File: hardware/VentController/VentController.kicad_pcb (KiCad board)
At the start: 2 copper layers, 18 parts, among them J1 AM2301B, J2 Conn_01x02, Q1 Q_NPN_EBC, U1 ATtiny85-20P

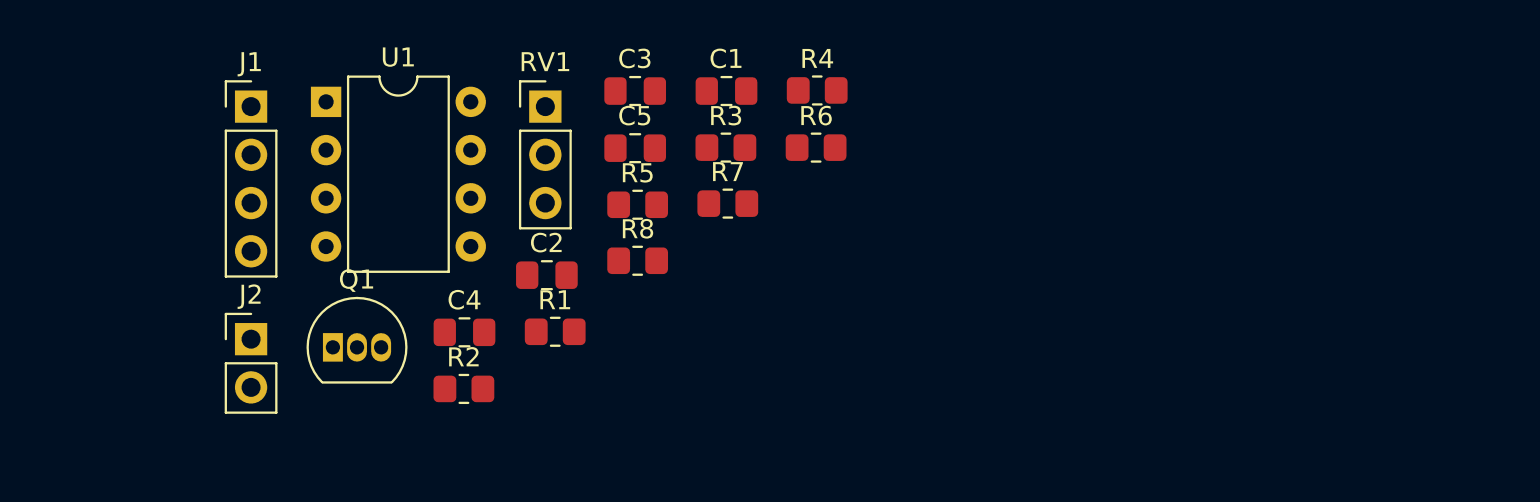
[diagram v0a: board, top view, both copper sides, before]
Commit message: Set pcb board edges
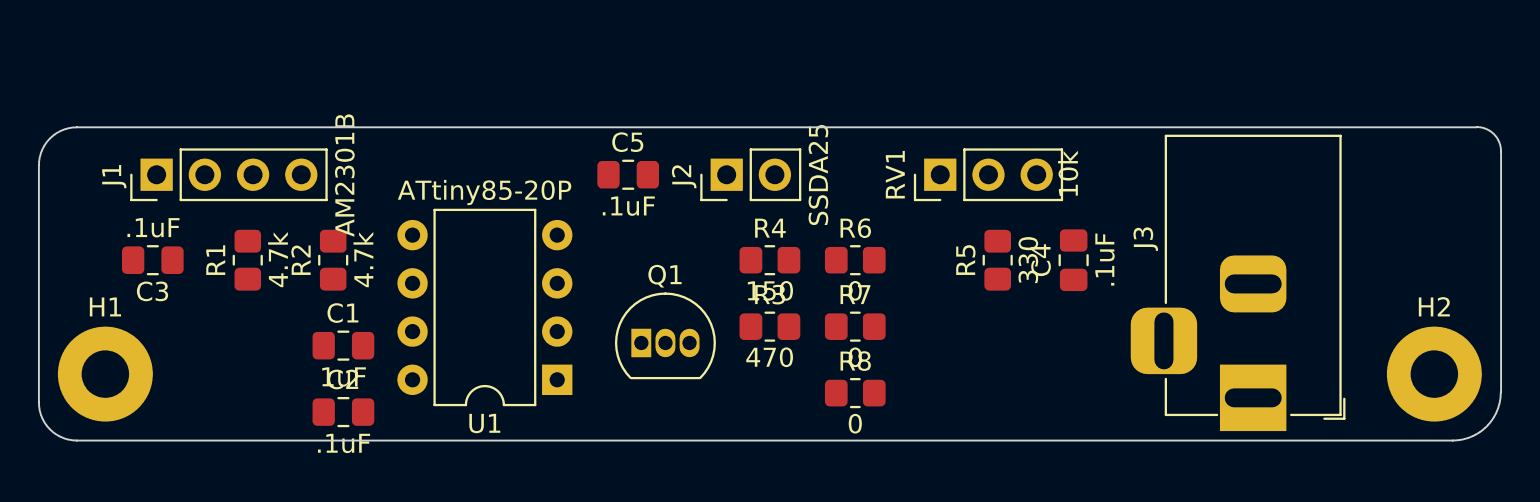
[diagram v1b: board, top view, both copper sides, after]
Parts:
- added H1: MountingHole_Pad, MountingHole:MountingHole_2.5mm_Pad, F.Cu at (100.0, 100.0)
- added H2: MountingHole_Pad, MountingHole:MountingHole_2.5mm_Pad, F.Cu at (170.0, 100.0)
- added J3: Barrel_Jack_Switch, Connector_BarrelJack:BarrelJack_Horizontal, F.Cu at (160.5, 101.2)
- J2: value Conn_01x02 -> SSDA25
- moved C4 32.3 mm to (151.0, 94.0), turned to 90 degrees
- moved C3 26.9 mm to (102.5, 94.0), turned to 180 degrees
- moved J2 26.5 mm to (132.7, 89.5), turned to 90 degrees
- moved C1 24.2 mm to (112.5, 98.5)
- moved RV1 21.1 mm to (144.0, 89.5), turned to 90 degrees
- moved R5 19.2 mm to (147.0, 94.0), turned to 90 degrees
- moved U1 19.0 mm to (123.8, 100.3), turned to 180 degrees
- moved R1 16.6 mm to (107.5, 94.0), turned to 90 degrees
- moved Q1 16.2 mm to (128.2, 98.4)
- moved R8 13.4 mm to (139.5, 101.0)
- moved C2 12.9 mm to (112.5, 102.0)
- moved R3 9.71 mm to (135.0, 97.5)
- moved R2 9.66 mm to (112.0, 94.0), turned to 90 degrees
- moved R7 9.33 mm to (139.5, 97.5)
- moved R4 9.28 mm to (135.0, 94.0)
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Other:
- board outline added: 77 x 16.5 mm

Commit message: Lay out pcb
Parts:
- J2: value SSDA25 -> Conn_01x02
- moved R3 3.50 mm to (135.0, 101.0)
- moved R4 2.00 mm to (135.0, 96.0)
- moved J1 1.50 mm to (101.2, 89.5)
- moved R5 1.00 mm to (146.0, 94.0)
- moved C3 0.50 mm to (102.0, 94.0)
- moved R1 0.50 mm to (107.0, 94.0)
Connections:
- J1 pad 2: /SDA -> /SCL
- J1 pad 3: /SCL -> /SDA
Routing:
- net VCC: track 0.00 -> 94.9 mm
- net Net-(RV1-Pad2): track 0.00 -> 33.8 mm, vias 0 -> 2
- net Net-(Q1-Pad3): track 0.00 -> 21.8 mm
- net Net-(J2-Pad2): track 0.00 -> 21.7 mm
- net /SCL: track 0.00 -> 16.1 mm
- net Net-(R3-Pad1): track 0.00 -> 13.0 mm
- net /SDA: track 0.00 -> 11.5 mm
- net Net-(J2-Pad1): track 0.00 -> 11.2 mm
- net Net-(Q1-Pad2): track 0.00 -> 7.97 mm
- net Net-(R5-Pad2): track 0.00 -> 4.78 mm
- net GND: vias 0 -> 51
- added copper zone on B.Cu, net GND
- added copper zone on F.Cu, net GND

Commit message: Finishing touches
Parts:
- J2: value Conn_01x02 -> SSRDA25
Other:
- board text added: "BathVent Grant Cooksey v1.0.0"
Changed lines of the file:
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@@
       (effects (font (size 1 1) (thickness 0.15)))
     )
-    (fp_text value "Conn_01x02" (at -3 1.275 180) (layer "F.SilkS")
+    (fp_text value "SSRDA25" (at -3 1.275 180) (layer "F.SilkS")
       (effects (font (size 1 1) (thickness 0.15)))
     )
@@
   (gr_arc (start 173.5 100.965) (mid 172.757516 102.757516) (end 170.965 103.5) (layer "Edge.Cuts") (width 0.1))
   (gr_arc (start 96.5 89) (mid 97.085786 87.585786) (end 98.5 87) (layer "Edge.Cuts") (width 0.1))
+  (gr_text "BathVent\nGrant Cooksey\nv1.0.0" (at 144.5 101) (layer "F.SilkS")
+    (effects (font (size 1 1) (thickness 0.15)) (justify left))
+  )
   (dimension (type aligned) (layer "Dwgs.User")
     (pts (xy 170 100) (xy 170 109.22))

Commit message: Feedback from board
* Added power led
* Updated text
* Adjusted mounting hole layout
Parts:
- added D1: LED, LED_SMD:LED_0805_2012Metric_Pad1.15x1.40mm_HandSolder, F.Cu at (119.0, 58.5)
- added R9: 330, Resistor_SMD:R_0805_2012Metric_Pad1.20x1.40mm_HandSolder, F.Cu at (119.0, 62.8)
- J2: value SSRDA25 -> SSR-25
- moved C4 48.1 mm to (111.7, 66.3), turned to 180 degrees
- moved H2 47.6 mm to (134.0, 68.8)
- moved J1 47.1 mm to (65.9, 58.3)
- moved J3 47.1 mm to (125.2, 70.0)
- moved C1 47.1 mm to (77.3, 67.3)
- moved C2 47.1 mm to (77.3, 70.8)
- moved C3 47.1 mm to (66.7, 62.8)
- moved C5 47.1 mm to (92.3, 58.3)
- moved J2 47.1 mm to (97.5, 58.3)
- moved Q1 47.1 mm to (93.0, 67.1)
- moved R1 47.1 mm to (71.7, 62.8)
- moved R2 47.1 mm to (76.7, 62.8)
- moved R3 47.1 mm to (99.7, 69.8)
- moved R4 47.1 mm to (99.7, 64.8)
- moved R5 47.1 mm to (110.7, 62.8)
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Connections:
- net /SCL renamed /SCL White
- net /SDA renamed /SDA Yellow
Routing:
- net VCC: track 94.9 -> 97.7 mm
- net Net-(D1-Pad2): track 0.00 -> 2.23 mm
- net GND: vias 51 -> 52
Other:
- board text added: "+"
- board text added: "-"
- board text added: "B"
- board text added: "GND"
- board text added: "R"
- board text added: "W"

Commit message: Bump board version text
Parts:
- moved C1 0.21 mm to (77.3, 67.5)
- moved C2 0.21 mm to (77.3, 71.0)
- moved C3 0.21 mm to (66.7, 63.0)
- moved C4 0.21 mm to (111.7, 66.5)
- moved C5 0.21 mm to (92.3, 58.5)
- moved D1 0.21 mm to (119.0, 58.8)
- moved H1 0.21 mm to (65.5, 69.0)
- moved H2 0.21 mm to (134.0, 69.0)
- moved J1 0.21 mm to (65.9, 58.5)
- moved J2 0.21 mm to (97.5, 58.5)
- moved J3 0.21 mm to (125.2, 70.2)
- moved Q1 0.21 mm to (93.0, 67.4)
- moved R1 0.21 mm to (71.7, 63.0)
- moved R2 0.21 mm to (76.7, 63.0)
- moved R3 0.21 mm to (99.7, 70.0)
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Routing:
- net GND: vias 52 -> 57
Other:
- board text added: "BathVent Grant Cooksey ${REVISION}"
- board text added: "Y"
- board text removed: "BathVent Grant Cooksey v1.0.0"
